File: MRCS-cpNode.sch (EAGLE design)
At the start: 45 parts, among them P1 CA CC, U1 MAX3465CPD, U2 NE555P

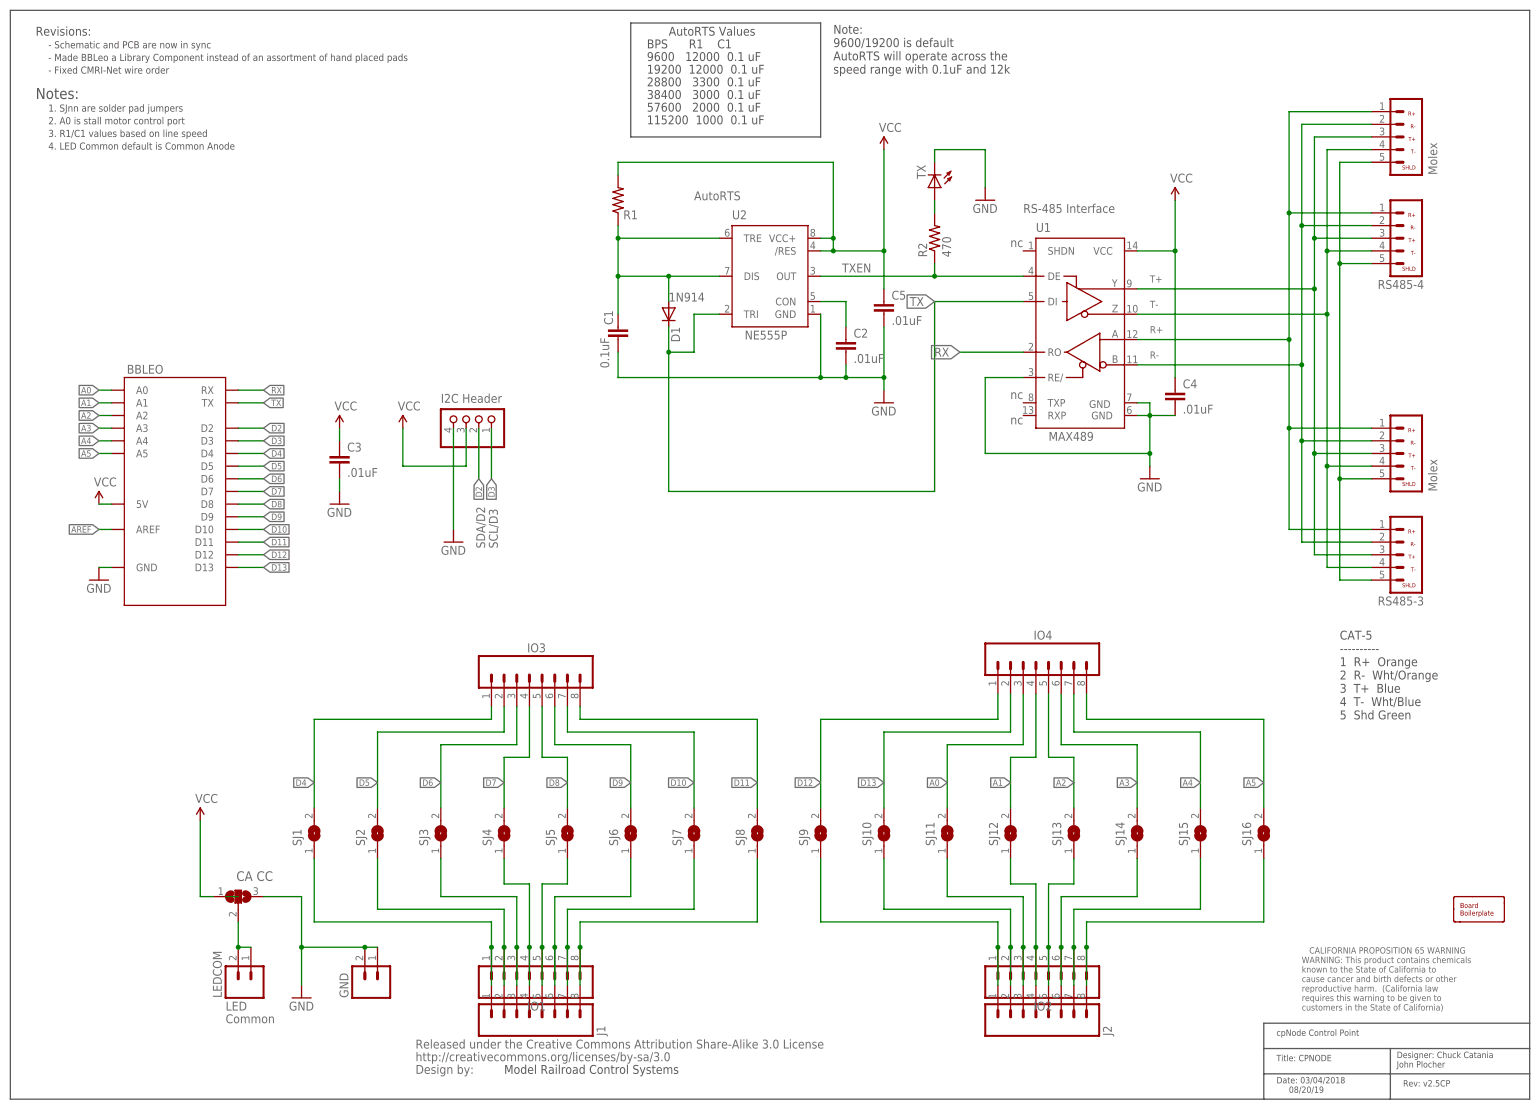
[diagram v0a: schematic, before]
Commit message: added 6-pin headers, fixed DCR errors
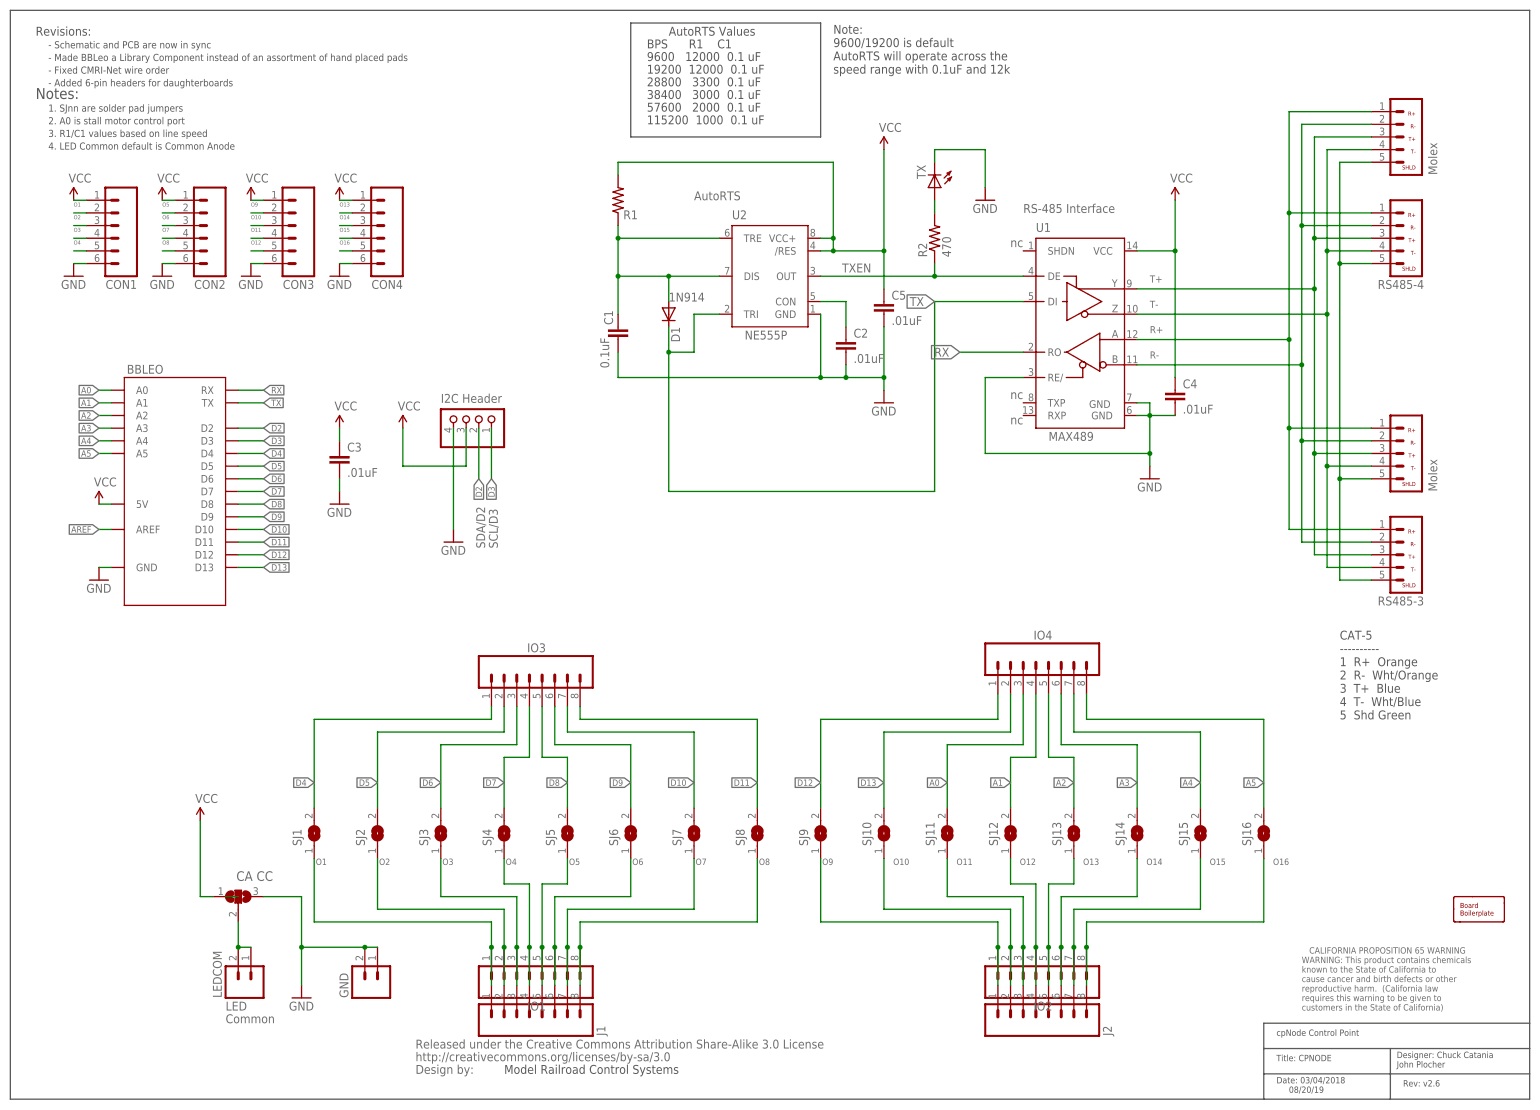
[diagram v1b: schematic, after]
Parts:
- added CON1, CON2, CON3, CON4: (no value), SPCoast:CONNECTOR-M06SIP_LOCK
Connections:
- removed net N$1: IO1.2, J1.2, SJ2.1
- removed net N$10: IO2.2, J2.2, SJ10.1
- removed net N$2: IO1.1, J1.1, SJ1.1
- removed net N$21: IO2.4, J2.4, SJ12.1
- removed net N$3: IO1.3, J1.3, SJ3.1
- removed net N$30: IO2.5, J2.5, SJ13.1
- removed net N$31: IO2.6, J2.6, SJ14.1
- removed net N$32: IO2.7, J2.7, SJ15.1
- removed net N$33: IO2.8, J2.8, SJ16.1
- removed net N$4: IO1.4, J1.4, SJ4.1
- removed net N$43: IO2.3, J2.3, SJ11.1
- removed net N$5: IO1.5, J1.5, SJ5.1
- removed net N$6: IO1.6, J1.6, SJ6.1
- removed net N$7: IO1.7, J1.7, SJ7.1
- removed net N$8: IO1.8, J1.8, SJ8.1
- removed net N$9: IO2.1, J2.1, SJ9.1
- new net O1: CON1.2, IO1.1, J1.1, SJ1.1
- new net O10: CON3.3, IO2.2, J2.2, SJ10.1
- new net O11: CON3.4, IO2.3, J2.3, SJ11.1
- new net O12: CON3.5, IO2.4, J2.4, SJ12.1
- new net O13: CON4.2, IO2.5, J2.5, SJ13.1
- new net O14: CON4.3, IO2.6, J2.6, SJ14.1
- new net O15: CON4.4, IO2.7, J2.7, SJ15.1
- new net O16: CON4.5, IO2.8, J2.8, SJ16.1
- new net O2: CON1.3, IO1.2, J1.2, SJ2.1
- new net O3: CON1.4, IO1.3, J1.3, SJ3.1
- new net O4: CON1.5, IO1.4, J1.4, SJ4.1
- new net O5: CON2.2, IO1.5, J1.5, SJ5.1
- new net O6: CON2.3, IO1.6, J1.6, SJ6.1
- new net O7: CON2.4, IO1.7, J1.7, SJ7.1
- new net O8: CON2.5, IO1.8, J1.8, SJ8.1
- new net O9: CON3.2, IO2.1, J2.1, SJ9.1
- net GND: now also CON1.6, CON2.6, CON3.6, CON4.6
- net VCC: now also CON1.1, CON2.1, CON3.1, CON4.1
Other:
- note added: "- Added 6-pin headers for daughterboards"
- note added: "Rev: v2.6"
- note removed: "Rev: v2.5CP"

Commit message: added missing values
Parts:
- BBLEO: value (none) -> Footprint
- CON1, CON2, CON3, CON4, GND, IO1, IO2, IO3, IO4, J1, J2, LEDCOM: value (none) -> 0.100
- R1: value (none) -> 12k
- SJ1, SJ10, SJ11, SJ12, SJ13, SJ14, SJ15, SJ16, SJ2, SJ3, SJ4, SJ5, SJ6, SJ7, SJ8, SJ9: value (none) -> OFF
- TX: value (none) -> G
- U$2: value CA-PROP65WARNING -> Prop65
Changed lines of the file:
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@@
 </classes>
 <parts>
-<part name="SJ1" library="jumper" deviceset="SJ" device=""/>
-<part name="SJ2" library="jumper" deviceset="SJ" device=""/>
-<part name="SJ3" library="jumper" deviceset="SJ" device=""/>
-<part name="SJ4" library="jumper" deviceset="SJ" device=""/>
-<part name="SJ5" library="jumper" deviceset="SJ" device=""/>
-<part name="SJ6" library="jumper" deviceset="SJ" device=""/>
-<part name="SJ7" library="jumper" deviceset="SJ" device=""/>
-<part name="SJ8" library="jumper" deviceset="SJ" device=""/>
-<part name="SJ9" library="jumper" deviceset="SJ" device=""/>
-<part name="SJ10" library="jumper" deviceset="SJ" device=""/>
+<part name="SJ1" library="jumper" deviceset="SJ" device="" value="OFF"/>
+<part name="SJ2" library="jumper" deviceset="SJ" device="" value="OFF"/>
+<part name="SJ3" library="jumper" deviceset="SJ" device="" value="OFF"/>
+<part name="SJ4" library="jumper" deviceset="SJ" device="" value="OFF"/>
+<part name="SJ5" library="jumper" deviceset="SJ" device="" value="OFF"/>
+<part name="SJ6" library="jumper" deviceset="SJ" device="" value="OFF"/>
+<part name="SJ7" library="jumper" deviceset="SJ" device="" value="OFF"/>
+<part name="SJ8" library="jumper" deviceset="SJ" device="" value="OFF"/>
+<part name="SJ9" library="jumper" deviceset="SJ" device="" value="OFF"/>
+<part name="SJ10" library="jumper" deviceset="SJ" device="" value="OFF"/>
 <part name="U2" library="SparkFun" deviceset="NE555" device="P"/>
 <part name="U1" library="maxim" deviceset="MAX346*" device="PD" technology="5C"/>
@@
 <part name="C2" library="SparkFun" deviceset="CAP" device="PTH2" value=".01uF"/>
 <part name="C3" library="SparkFun" deviceset="CAP" device="PTH2" value=".01uF"/>
-<part name="R1" library="SparkFun" deviceset="RESISTOR" device="PTH-1/4W"/>
+<part name="R1" library="SparkFun" deviceset="RESISTOR" device="PTH-1/4W" value="12k"/>
 <part name="D1" library="diode" deviceset="1N4148" device="DO35-10"/>
-<part name="SJ11" library="jumper" deviceset="SJ" device=""/>
-<part name="SJ12" library="jumper" deviceset="SJ" device=""/>
-<part name="SJ13" library="jumper" deviceset="SJ" device=""/>
-<part name="SJ14" library="jumper" deviceset="SJ" device=""/>
-<part name="SJ15" library="jumper" deviceset="SJ" device=""/>
-<part name="SJ16" library="jumper" deviceset="SJ" device=""/>
-<part name="IO1" library="SparkFun" deviceset="M08" device="1X08"/>
-<part name="IO2" library="SparkFun" deviceset="M08" device="1X08"/>
-<part name="LEDCOM" library="SparkFun" deviceset="M02" device="POLAR_LOCK"/>
+<part name="SJ11" library="jumper" deviceset="SJ" device="" value="OFF"/>
+<part name="SJ12" library="jumper" deviceset="SJ" device="" value="OFF"/>
+<part name="SJ13" library="jumper" deviceset="SJ" device="" value="OFF"/>
+<part name="SJ14" library="jumper" deviceset="SJ" device="" value="OFF"/>
+<part name="SJ15" library="jumper" deviceset="SJ" device="" value="OFF"/>
+<part name="SJ16" library="jumper" deviceset="SJ" device="" value="OFF"/>
+<part name="IO1" library="SparkFun" deviceset="M08" device="1X08" value="0.100"/>
+<part name="IO2" library="SparkFun" deviceset="M08" device="1X08" value="0.100"/>
+<part name="LEDCOM" library="SparkFun" deviceset="M02" device="POLAR_LOCK" value="0.100"/>
 <part name="P+1" library="SparkFun" deviceset="VCC" device=""/>
 <part name="GND2" library="SparkFun" deviceset="GND" device=""/>
@@
 <part name="C5" library="SparkFun" deviceset="CAP" device="PTH2" value=".01uF"/>
 <part name="R2" library="SparkFun" deviceset="RESISTOR" device="PTH-1/4W" value="470"/>
-<part name="GND" library="SparkFun" deviceset="M02" device="POLAR_LOCK"/>
+<part name="GND" library="SparkFun" deviceset="M02" device="POLAR_LOCK" value="0.100"/>
 <part name="P1" library="Discreter" deviceset="PAD-SOLDERJUMPER-2WAY" device="T" value="CA   CC"/>
 <part name="P+7" library="SparkFun" deviceset="VCC" device=""/>
 <part name="GND9" library="SparkFun" deviceset="GND" device=""/>
 <part name="U$1" library="SparkFun" deviceset="CREATIVE_COMMONS" device=""/>
-<part name="U$2" library="MRCS-prop65warningTop" deviceset="CA-PROP65WARNING" device=""/>
+<part name="U$2" library="MRCS-prop65warningTop" deviceset="CA-PROP65WARNING" device="" value="Prop65"/>
 <part name="RS485-4" library="SPCoast" deviceset="CONNECTOR-CMRINET" device="3.5MM" value="3.5mm"/>
 <part name="RS485-1" library="SPCoast" deviceset="CONNECTOR-CMRINET" device=".156" value="Molex"/>
 <part name="RS485-2" library="SPCoast" deviceset="CONNECTOR-CMRINET" device=".156" value="Molex"/>
-<part name="TX" library="SparkFun-LED" deviceset="LED" device="3MM"/>
+<part name="TX" library="SparkFun-LED" deviceset="LED" device="3MM" value="G"/>
 <part name="BOARD1" library="SPCoast" deviceset="BOARD" device="69X100MRCS"/>
-<part name="BBLEO" library="SPCoast" deviceset="ARDUINO-BBLEO" device=""/>
+<part name="BBLEO" library="SPCoast" deviceset="ARDUINO-BBLEO" device="" value="Footprint"/>
 <part name="GND5" library="SparkFun" deviceset="GND" device=""/>
 <part name="P+5" library="SparkFun" deviceset="VCC" device=""/>
 <part name="GND6" library="SparkFun" deviceset="GND" device=""/>
 <part name="P+6" library="SparkFun" deviceset="VCC" device=""/>
-<part name="IO3" library="SparkFun" deviceset="M08" device="1X08"/>
-<part name="IO4" library="SparkFun" deviceset="M08" device="1X08"/>
-<part name="J1" library="SPCoast" deviceset="CONNECTOR-M08" device="LOCK_LONGPADS"/>
-<part name="J2" library="SPCoast" deviceset="CONNECTOR-M08" device="LOCK_LONGPADS"/>
+<part name="IO3" library="SparkFun" deviceset="M08" device="1X08" value="0.100"/>
+<part name="IO4" library="SparkFun" deviceset="M08" device="1X08" value="0.100"/>
+<part name="J1" library="SPCoast" deviceset="CONNECTOR-M08" device="LOCK_LONGPADS" value="0.100"/>
+<part name="J2" library="SPCoast" deviceset="CONNECTOR-M08" device="LOCK_LONGPADS" value="0.100"/>
 <part name="RS485-3" library="SPCoast" deviceset="CONNECTOR-CMRINET" device="3.5MM" value="3.5mm"/>
-<part name="CON1" library="SPCoast" deviceset="CONNECTOR-M06" device="SIP_LOCK"/>
-<part name="CON2" library="SPCoast" deviceset="CONNECTOR-M06" device="SIP_LOCK"/>
-<part name="CON3" library="SPCoast" deviceset="CONNECTOR-M06" device="SIP_LOCK"/>
-<part name="CON4" library="SPCoast" deviceset="CONNECTOR-M06" device="SIP_LOCK"/>
+<part name="CON1" library="SPCoast" deviceset="CONNECTOR-M06" device="SIP_LOCK" value="0.100"/>
+<part name="CON2" library="SPCoast" deviceset="CONNECTOR-M06" device="SIP_LOCK" value="0.100"/>
+<part name="CON3" library="SPCoast" deviceset="CONNECTOR-M06" device="SIP_LOCK" value="0.100"/>
+<part name="CON4" library="SPCoast" deviceset="CONNECTOR-M06" device="SIP_LOCK" value="0.100"/>
 <part name="P+3" library="SparkFun" deviceset="VCC" device=""/>
 <part name="P+8" library="SparkFun" deviceset="VCC" device=""/>

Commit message: added missing values
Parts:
- I2CHDR: value (none) -> 0.100
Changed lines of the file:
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@@
 <part name="P+2" library="SparkFun" deviceset="VCC" device=""/>
 <part name="GND3" library="SparkFun" deviceset="GND" device=""/>
-<part name="I2CHDR" library="pinhead" deviceset="PINHD-1X4" device="/90"/>
+<part name="I2CHDR" library="pinhead" deviceset="PINHD-1X4" device="/90" value="0.100"/>
 <part name="GND8" library="SparkFun" deviceset="GND" device=""/>
 <part name="P+4" library="SparkFun" deviceset="VCC" device=""/>

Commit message: normalized values
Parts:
- BOARD1: value BOARD69X100MRCS -> BOARD
- C1: device SparkFun:CAPPTH2 -> SPCoast:CAPPTH2
- C2, C3, C4, C5: value .01uF -> 0.01uF; device SparkFun:CAPPTH2 -> SPCoast:CAPPTH2
- D1: value 1N4148DO35-10 -> 1N4148; device diode:1N4148DO35-10 -> SPCoast:DIODE1N4148
- R1, R2: device SparkFun:RESISTORPTH-1/4W -> SPCoast:RPTH04
- RS485-1, RS485-2: value Molex -> 0.156
- TX: device SparkFun-LED:LED3MM -> SPCoast:LEDLED3MM

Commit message: silk and trace cleanup
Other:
- note added: "Rev: v2.7"
- note removed: "Rev: v2.6"
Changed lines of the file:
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@@
 <layer number="255" name="routoute" color="7" fill="1" visible="yes" active="yes"/>
 </layers>
-<schematic xreflabel="%F%N/%S.%C%R" xrefpart="/%S.%C%R">
+<schematic xreflabel="%F%N/%S" xrefpart="/%S.%C%R">
 <attributes>
 </attributes>
@@
 <wire x1="162.56" y1="215.9" x2="124.46" y2="215.9" width="0.1524" layer="97"/>
 <wire x1="124.46" y1="215.9" x2="124.46" y2="193.04" width="0.1524" layer="97"/>
-<text x="279.4" y="2.54" size="1.27" layer="97" font="vector">Rev: v2.6</text>
+<text x="279.4" y="2.54" size="1.27" layer="97" font="vector">Rev: v2.7</text>
 <text x="254" y="1.27" size="1.27" layer="97" font="vector">Date: 03/04/2018
      08/20/19</text>
